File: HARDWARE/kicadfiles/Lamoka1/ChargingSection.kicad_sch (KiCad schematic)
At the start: 48 parts, among them J2 BAT TEMP: 10k NTC B3435, Q6 SIR680LDP-T1-RE3, Q7 SIR680LDP-T1-RE3, Q8 SIR680LDP-T1-RE3, Q9 SIR680LDP-T1-RE3, U1 BQ25756RRVR

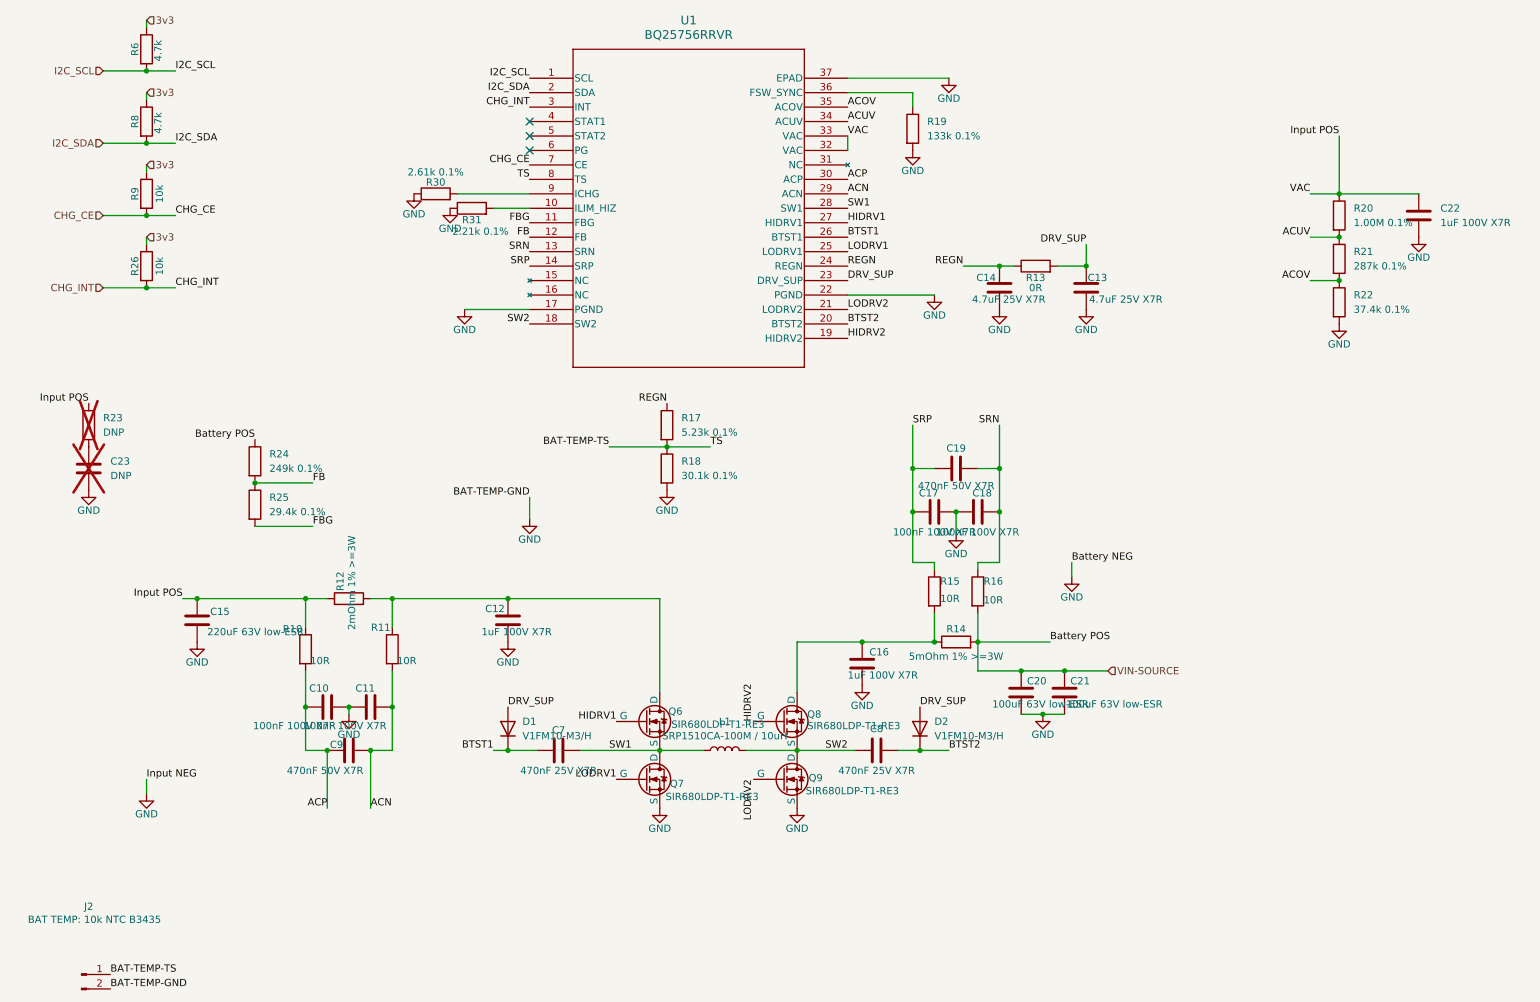
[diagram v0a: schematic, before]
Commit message: Improvement to charging section
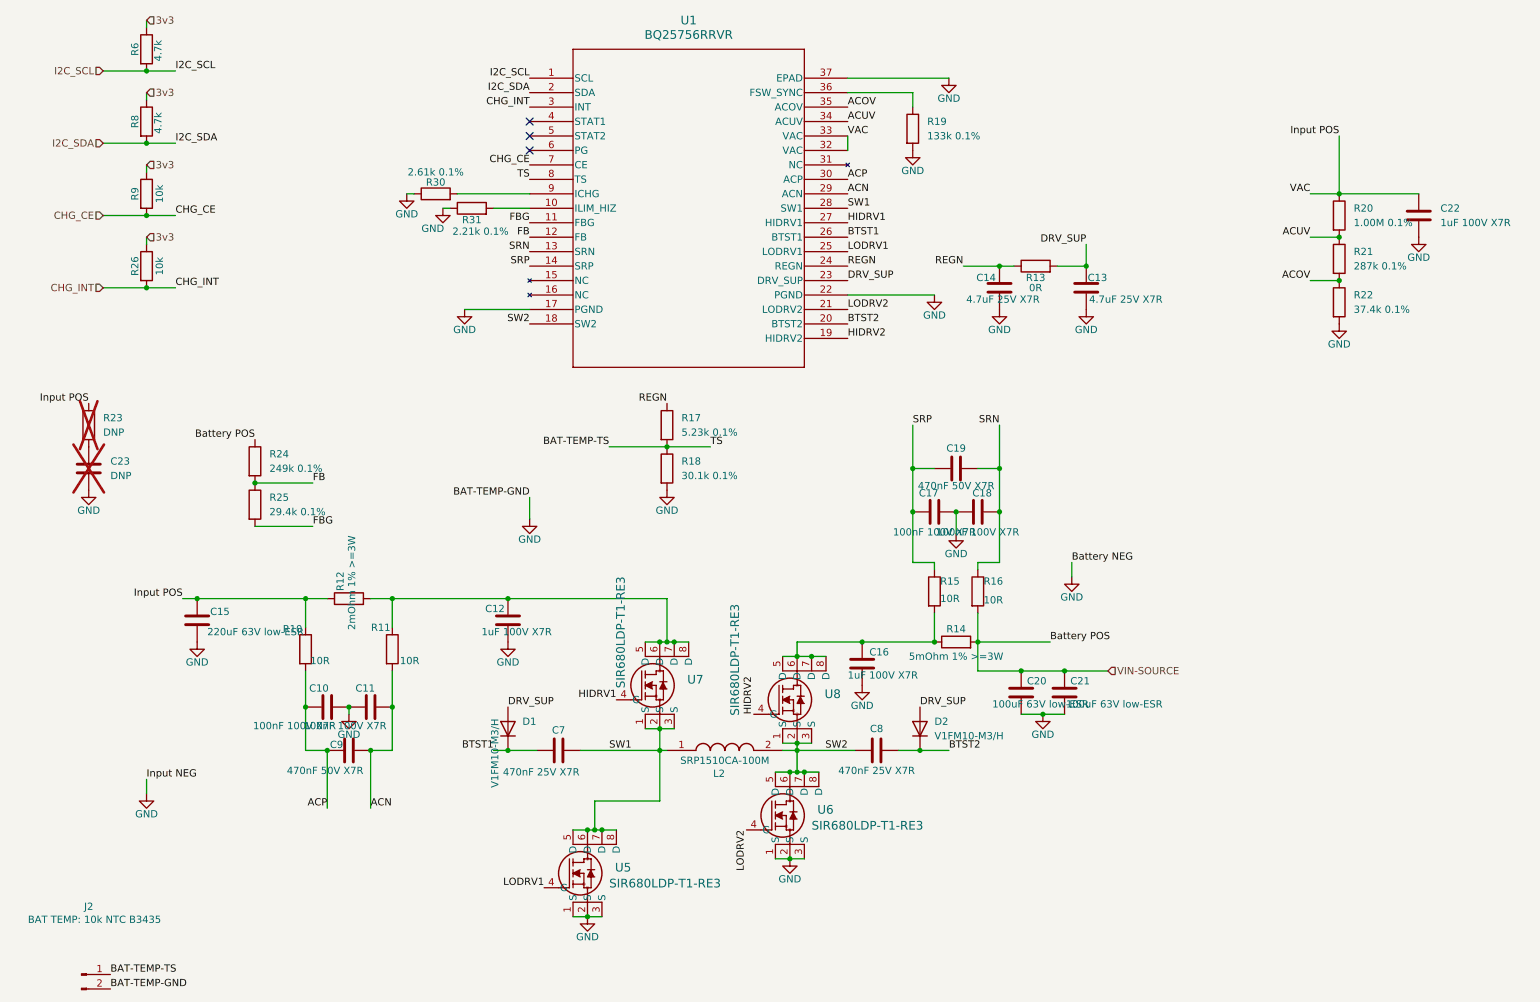
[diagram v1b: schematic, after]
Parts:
- removed L1: SRP1510CA-100M / 10uH, symbol Device:L
- removed Q6, Q7, Q8, Q9: SIR680LDP-T1-RE3, symbol Simulation_SPICE:NMOS
- added L2: SRP1510CA-100M, Components:SRP1510CA100M, symbol SRP1510CA-100M:SRP1510CA-100M
- added U5, U6, U7, U8: SIR680LDP-T1-RE3, Components:MOSFET_DP-T1-RE3_VIS, symbol 2026-07-24_20-06-52:SIR680LDP-T1-RE3
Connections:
- net GND: now also U5.1 (S), U5.2 (S), U5.3 (S), U6.1 (S), U6.2 (S), U6.3 (S)
- net HIDRV1: now also U7.4 (G)
- net HIDRV2: now also U8.4 (G)
- net LODRV1: now also U5.4 (G)
- net LODRV2: now also U6.4 (G)
- net SW1: now also L2.1, U5.5 (D), U5.6 (D), U5.7 (D), U5.8 (D), U7.1 (S), U7.2 (S), U7.3 (S)
- net SW2: now also L2.2, U6.5 (D), U6.6 (D), U6.7 (D), U6.8 (D), U8.1 (S), U8.2 (S), U8.3 (S)
- net at C12.2, R11.1, R12.2: now also U7.5 (D), U7.6 (D), U7.7 (D), U7.8 (D)
- net at C16.1, R14.1, R15.2: now also U8.5 (D), U8.6 (D), U8.7 (D), U8.8 (D)

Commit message: General improvements to the charging circuit
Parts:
- R12, R14: footprint (none) -> Components:CSSK3637_4Terminal_Kelvin
- renumbered U5 to Q6, U7 to Q7, U6 to Q8, U8 to Q9
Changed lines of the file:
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@@
 		(in_pos_files yes)
 		(dnp no)
-		(property "Reference" "U5"
-			(at 121.666 166.624 0)
+		(property "Reference" "Q6"
+			(at 120.904 166.624 0)
 			(show_name no)
 			(do_not_autoplace no)
@@
 			(project "Lamoka1"
 				(path "/50fe8bbc-b3f6-4de5-9677-9b5870b87390/fb4f0aa7-d40c-468b-b4b6-22d46a6e117f"
-					(reference "U5")
+					(reference "Q6")
 					(unit 1)
 				)
@@
 			)
 		)
-		(property "Footprint" ""
+		(property "Footprint" "Components:CSSK3637_4Terminal_Kelvin"
 			(at 74.93 121.158 90)
 			(hide yes)
@@
 		(in_pos_files yes)
 		(dnp no)
-		(property "Reference" "U8"
+		(property "Reference" "Q9"
 			(at 158.496 136.144 0)
 			(show_name no)
@@
 			(project "Lamoka1"
 				(path "/50fe8bbc-b3f6-4de5-9677-9b5870b87390/fb4f0aa7-d40c-468b-b4b6-22d46a6e117f"
-					(reference "U8")
+					(reference "Q9")
 					(unit 1)
 				)
@@
 		(in_pos_files yes)
 		(dnp no)
-		(property "Reference" "U7"
-			(at 134.366 133.604 0)
+		(property "Reference" "Q7"
+			(at 133.604 133.858 0)
 			(show_name no)
 			(do_not_autoplace no)
@@
 			(project "Lamoka1"
 				(path "/50fe8bbc-b3f6-4de5-9677-9b5870b87390/fb4f0aa7-d40c-468b-b4b6-22d46a6e117f"
-					(reference "U7")
+					(reference "Q7")
 					(unit 1)
 				)
@@
 			)
 		)
-		(property "Footprint" ""
+		(property "Footprint" "Components:CSSK3637_4Terminal_Kelvin"
 			(at 181.61 128.778 90)
 			(hide yes)
@@
 		(in_pos_files yes)
 		(dnp no)
-		(property "Reference" "U6"
+		(property "Reference" "Q8"
 			(at 157.226 156.464 0)
 			(show_name no)
@@
 			(project "Lamoka1"
 				(path "/50fe8bbc-b3f6-4de5-9677-9b5870b87390/fb4f0aa7-d40c-468b-b4b6-22d46a6e117f"
-					(reference "U6")
+					(reference "Q8")
 					(unit 1)
 				)

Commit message: FIX whole Lamoka1 general stuff
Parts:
- C15: footprint (none) -> Components:PCAP_10x10-ELECT_NCA
- C20, C21: footprint (none) -> Components:PCAP_8x10-ELECT_NCH
- J2: footprint (none) -> Connector_JST:JST_XH_B2B-XH-A_1x02_P2.50mm_Vertical
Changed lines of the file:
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@@
 			)
 		)
-		(property "Footprint" ""
+		(property "Footprint" "Components:PCAP_10x10-ELECT_NCA"
 			(at 49.2252 127 0)
 			(hide yes)
@@
 			)
 		)
-		(property "Footprint" ""
+		(property "Footprint" "Components:PCAP_8x10-ELECT_NCH"
 			(at 201.6252 139.7 0)
 			(hide yes)
@@
 			)
 		)
-		(property "Footprint" ""
+		(property "Footprint" "Connector_JST:JST_XH_B2B-XH-A_1x02_P2.50mm_Vertical"
 			(at 27.94 185.42 0)
 			(hide yes)
@@
 			)
 		)
-		(property "Footprint" ""
+		(property "Footprint" "Components:PCAP_8x10-ELECT_NCH"
 			(at 194.0052 139.7 0)
 			(hide yes)

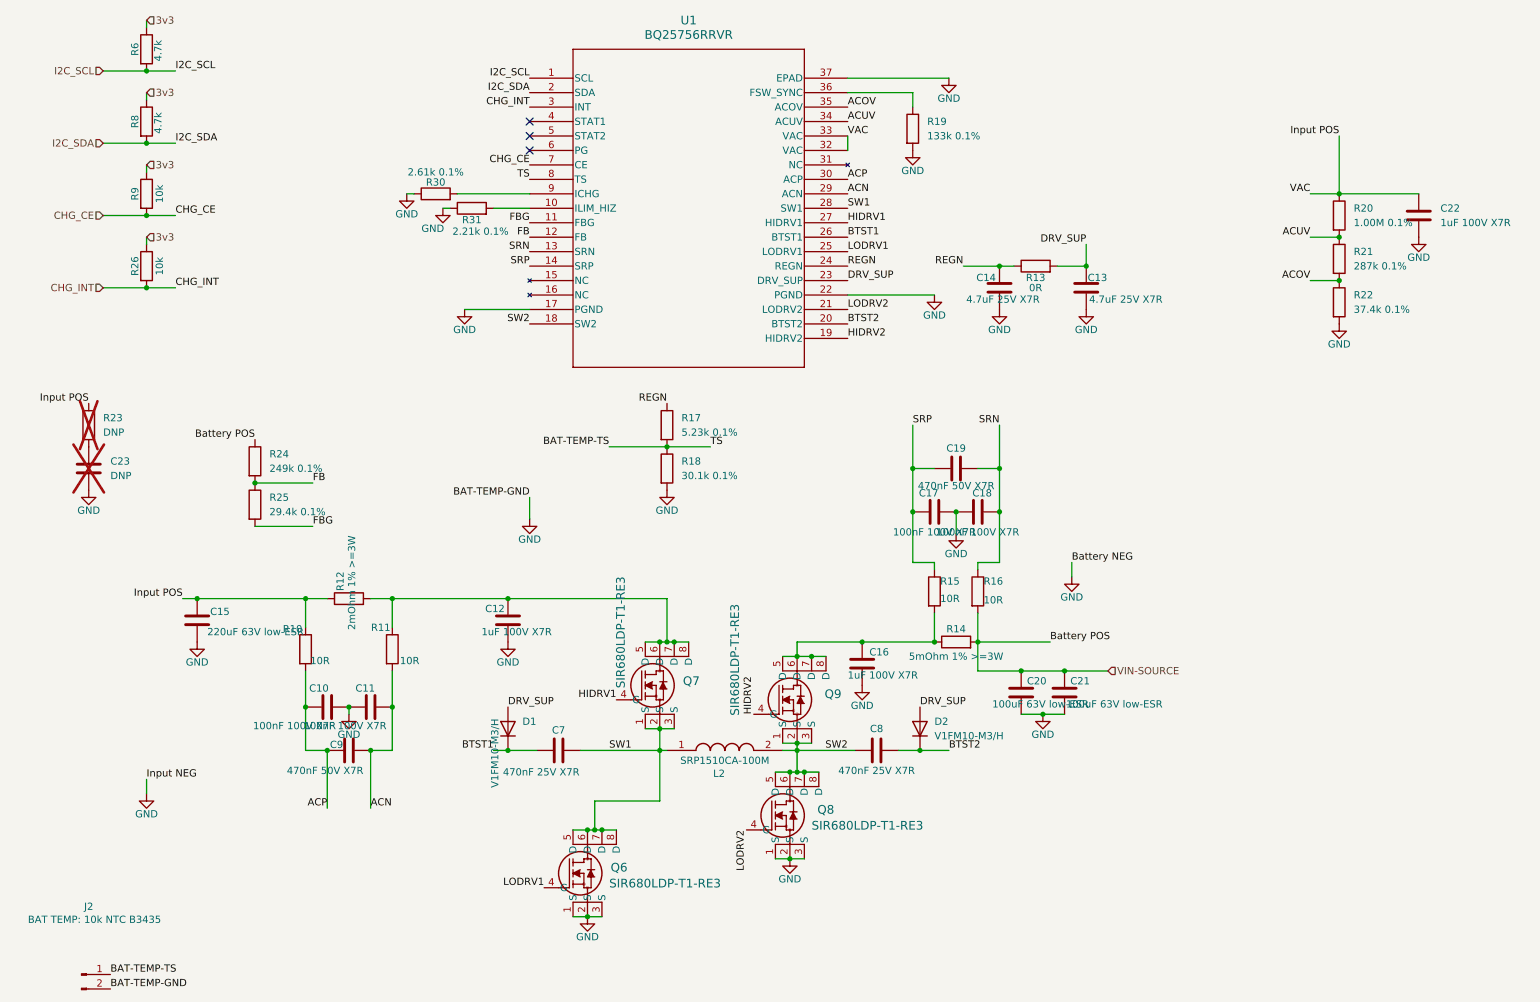
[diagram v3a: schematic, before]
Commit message: docs: Document prototype P1 schematic design improvements
Major updates to boost converter topology with LM5122 driver,
connect all section interfaces (charging, control), fix net connectivity.

This represents a near-complete functional schematic for the Lamoka1
inverter/charger system. All three main sections now have proper
interconnections for the RP2354A control implementation.
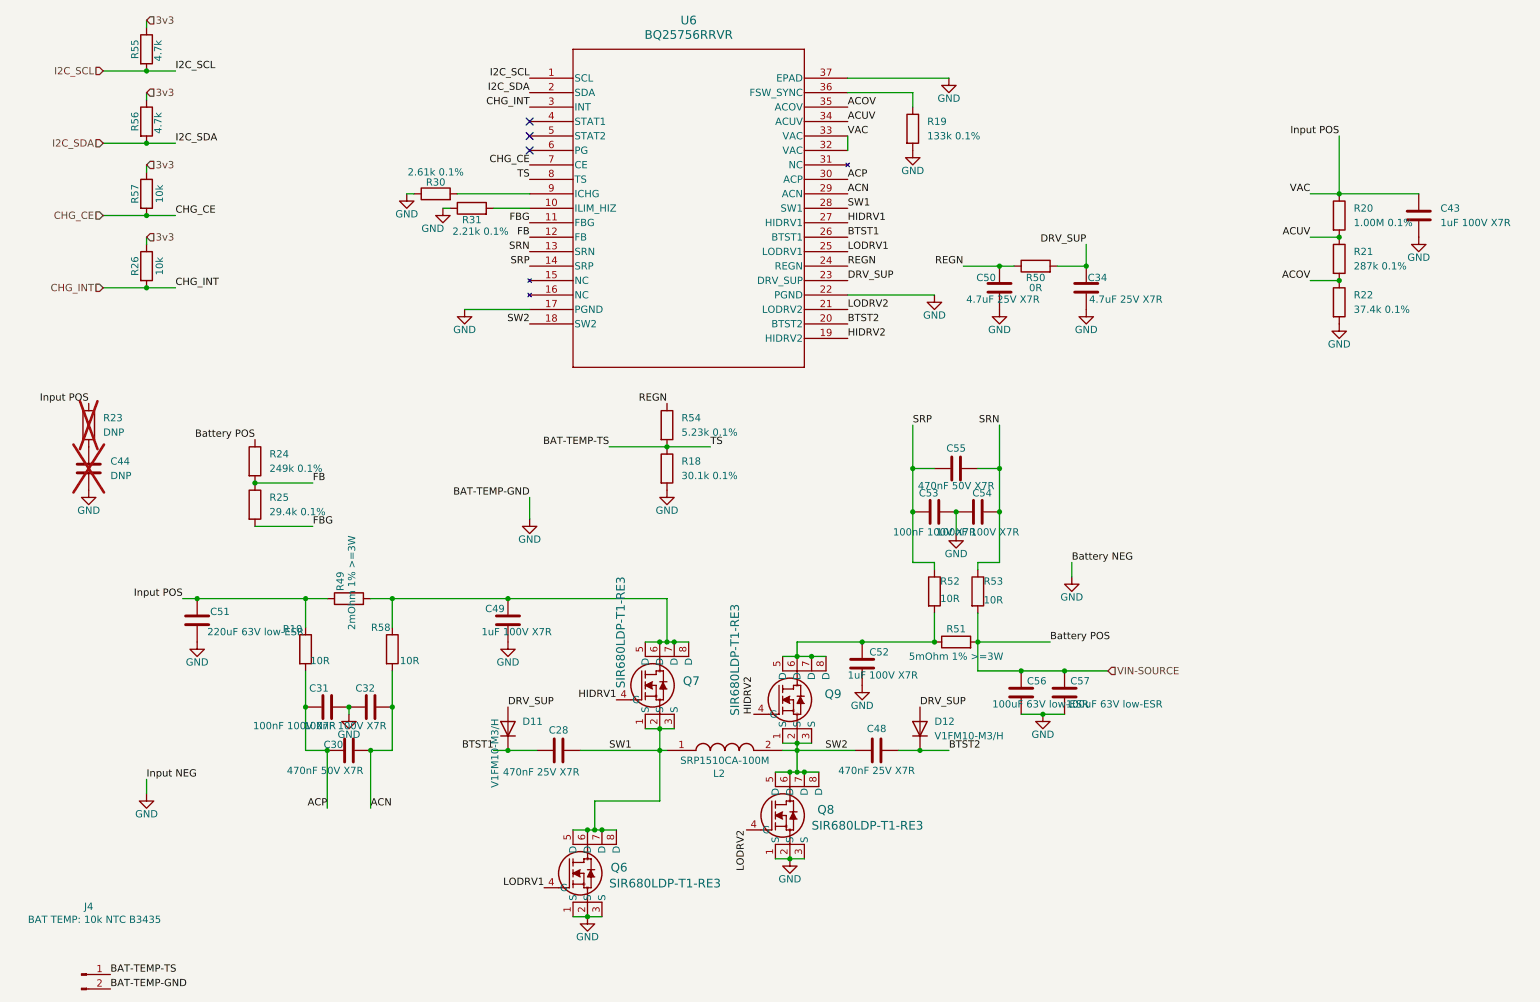
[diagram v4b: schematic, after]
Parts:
- renumbered C7 to C28, C9 to C30, C10 to C31, C11 to C32, C13 to C34, C22 to C43, C23 to C44, C8 to C48, C12 to C49, C14 to C50, C15 to C51, C16 to C52, C17 to C53, C18 to C54, C19 to C55, C20 to C56, C21 to C57, D1 to D11, D2 to D12, J2 to J4, R12 to R49, R13 to R50, R14 to R51, R15 to R52, R16 to R53, R17 to R54, R6 to R55, R8 to R56, R9 to R57, R11 to R58, U1 to U6

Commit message: Revert "docs: Document prototype P1 schematic design improvements"
This reverts commit 9a36aaba68a23f8da8ed8c8f957268abdd88419f.
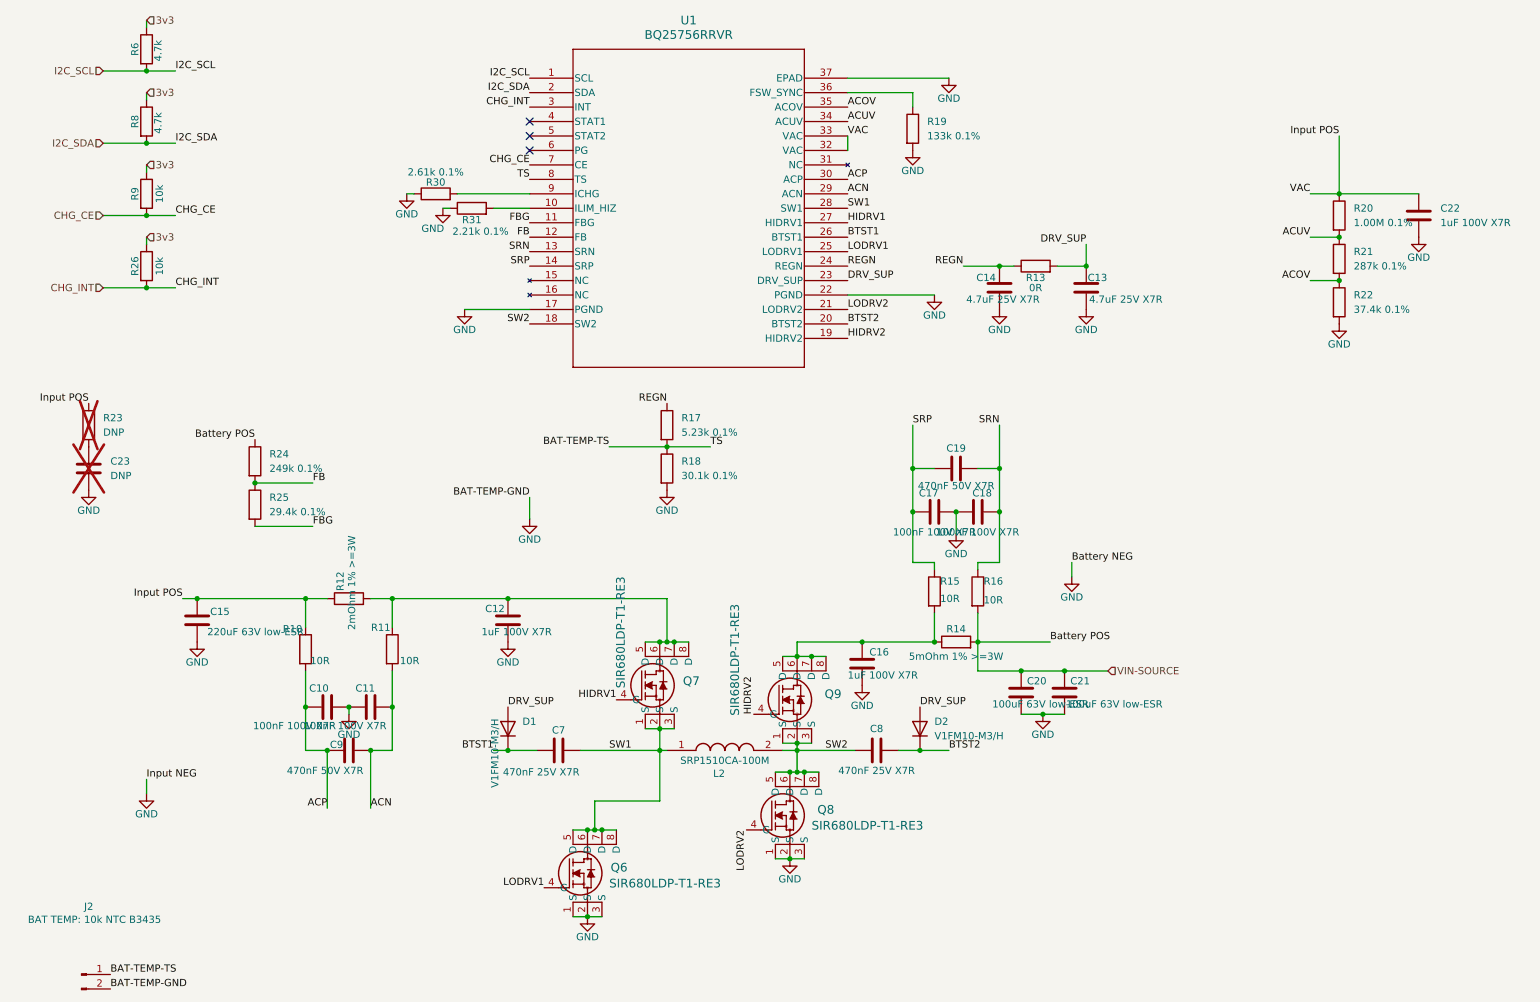
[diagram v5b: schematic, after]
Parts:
- renumbered C31 to C10, C32 to C11, C49 to C12, C34 to C13, C50 to C14, C51 to C15, C52 to C16, C53 to C17, C54 to C18, C55 to C19, C56 to C20, C57 to C21, C43 to C22, C44 to C23, C28 to C7, C48 to C8, C30 to C9, D11 to D1, D12 to D2, J4 to J2, R58 to R11, R49 to R12, R50 to R13, R51 to R14, R52 to R15, R53 to R16, R54 to R17, R55 to R6, R56 to R8, R57 to R9, U6 to U1
